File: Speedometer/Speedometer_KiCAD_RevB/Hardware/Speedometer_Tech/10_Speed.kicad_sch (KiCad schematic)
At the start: 14 parts, among them U100 TLC59108IPWR, U101 TLC59108IPWR, U102 TLC59108IPWR, U110 TLC59108IPWR, U111 TLC59108IPWR

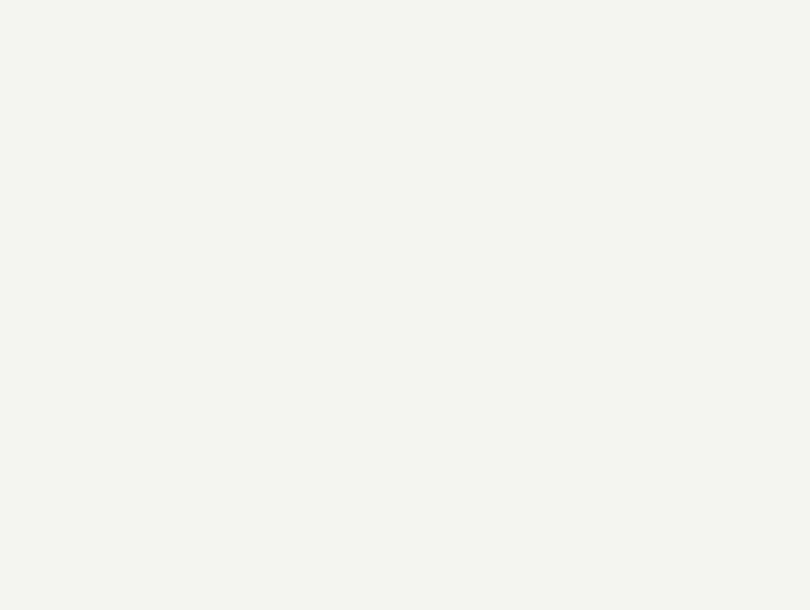
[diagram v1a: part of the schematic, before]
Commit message: current version of lada speedometer in kicad
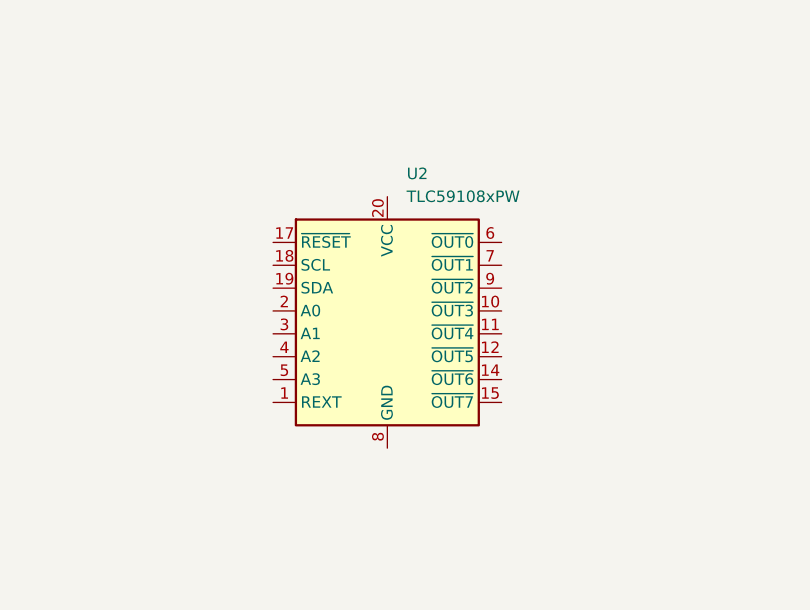
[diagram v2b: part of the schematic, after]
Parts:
- added U2: TLC59108xPW, Package_SO:TSSOP-20_4.4x6.5mm_P0.65mm, symbol Driver_LED:TLC59108xPW
- U100, U101, U102, U110, U111: footprint PW0020A_M -> Package_SO:TSSOP-20_4.4x6.5mm_P0.65mm
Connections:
- new net: U2.13 (GND), U2.16 (GND), U2.8 (GND)
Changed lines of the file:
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@@
 			)
 		)
-		(property "Footprint" "PW0020A_M"
+		(property "Footprint" "Package_SO:TSSOP-20_4.4x6.5mm_P0.65mm"
 			(at 68.58 109.0422 0)
 			(effects
@@
 			)
 		)
-		(property "Footprint" "PW0020A_M"
+		(property "Footprint" "Package_SO:TSSOP-20_4.4x6.5mm_P0.65mm"
 			(at 170.18 109.0422 0)
 			(effects
@@
 	)
 	(symbol
+		(lib_id "Driver_LED:TLC59108xPW")
+		(at 231.14 217.17 0)
+		(unit 1)
+		(exclude_from_sim no)
+		(in_bom yes)
+		(on_board yes)
+		(dnp no)
+		(fields_autoplaced yes)
+		(property "Reference" "U2"
+			(at 233.2833 199.39 0)
+			(effects
+				(font
+					(size 1.27 1.27)
+				)
+				(justify left)
+			)
+		)
+		(property "Value" "TLC59108xPW"
+			(at 233.2833 201.93 0)
+			(effects
+				(font
+					(size 1.27 1.27)
+				)
+				(justify left)
+			)
+		)
+		(property "Footprint" "Package_SO:TSSOP-20_4.4x6.5mm_P0.65mm"
+			(at 231.14 217.17 0)
+			(effects
+				(font
+					(size 1.27 1.27)
+				)
+				(hide yes)
+			)
+		)
+		(property "Datasheet" "https://www.ti.com/lit/ds/symlink/tlc59108.pdf"
+			(at 226.06 218.44 0)
+			(effects
+				(font
+					(size 1.27 1.27)
+				)
+				(hide yes)
+			)
+		)
+		(property "Description" "8-Channel, 8-Bit Fm+ I2C-Bus Constant-Current LED Sink Driver, TSSOP-20"
+			(at 231.14 217.17 0)
+			(effects
+				(font
+					(size 1.27 1.27)
+				)
+				(hide yes)
+			)
+		)
+		(pin "12"
+		)
+		(pin "8"
+		)
+		(pin "19"
+		)
+		(pin "2"
+		)
+		(pin "3"
+		)
+		(pin "4"
+		)
+		(pin "5"
+		)
+		(pin "1"
+		)
+		(pin "20"
+		)
+		(pin "13"
+		)
+		(pin "14"
+		)
+		(pin "10"
+		)
+		(pin "11"
+		)
+		(pin "9"
+		)
+		(pin "7"
+		)
+		(pin "6"
+		)
+		(pin "15"
+		)
+		(pin "17"
+		)
+		(pin "18"
+		)
+		(pin "16"
+		)
+		(instances
+			(project ""
+				(path "/7a911dfa-7957-409a-ad31-10c26a0bf949/7f25a167-5e25-4142-beba-23f2a558c57e"
+					(reference "U2")
+					(unit 1)
+				)
+			)
+		)
+	)
+	(symbol
 		(lib_id "Speedometer_Tech-altium-import:Designator_0_TI-TLC59108PW20")
 		(at 99.06 228.4222 0)
@@
 			)
 		)
-		(property "Footprint" "PW0020A_M"
+		(property "Footprint" "Package_SO:TSSOP-20_4.4x6.5mm_P0.65mm"
 			(at 99.06 228.4222 0)
 			(effects
@@
 			)
 		)
-		(property "Footprint" "PW0020A_M"
+		(property "Footprint" "Package_SO:TSSOP-20_4.4x6.5mm_P0.65mm"
 			(at 269.24 109.0422 0)
 			(effects
@@
 			)
 		)
-		(property "Footprint" "PW0020A_M"
+		(property "Footprint" "Package_SO:TSSOP-20_4.4x6.5mm_P0.65mm"
 			(at 99.06 190.3222 0)
 			(effects

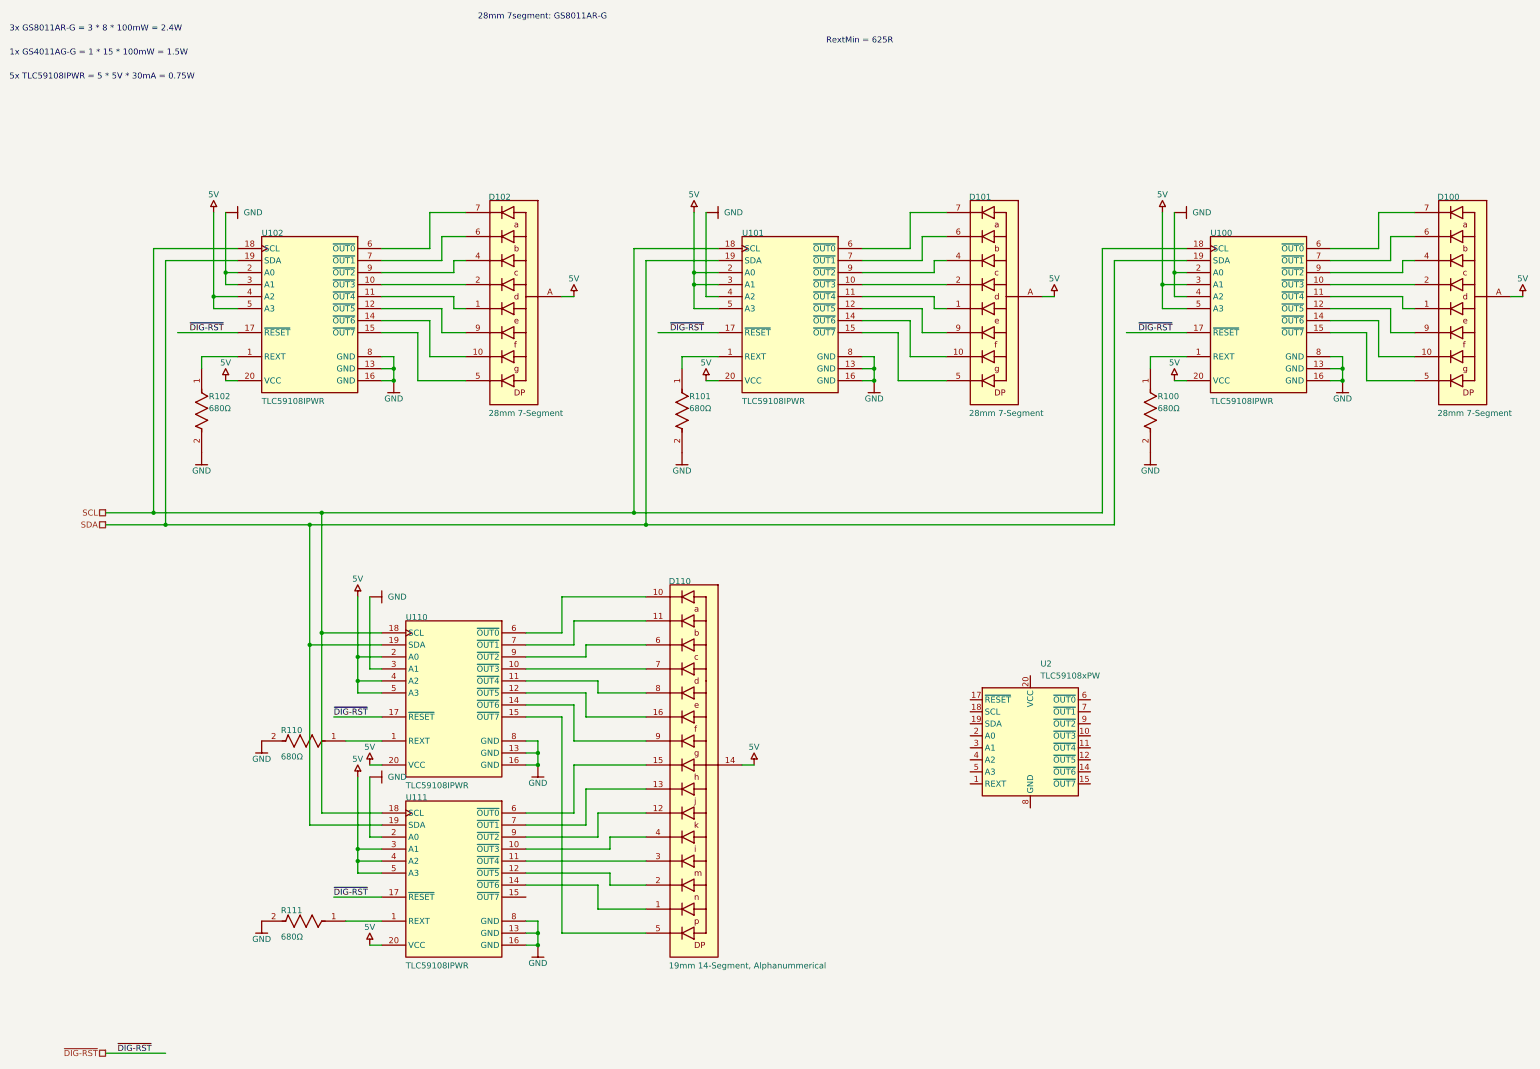
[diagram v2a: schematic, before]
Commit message: Speedometer DRC mostly passed
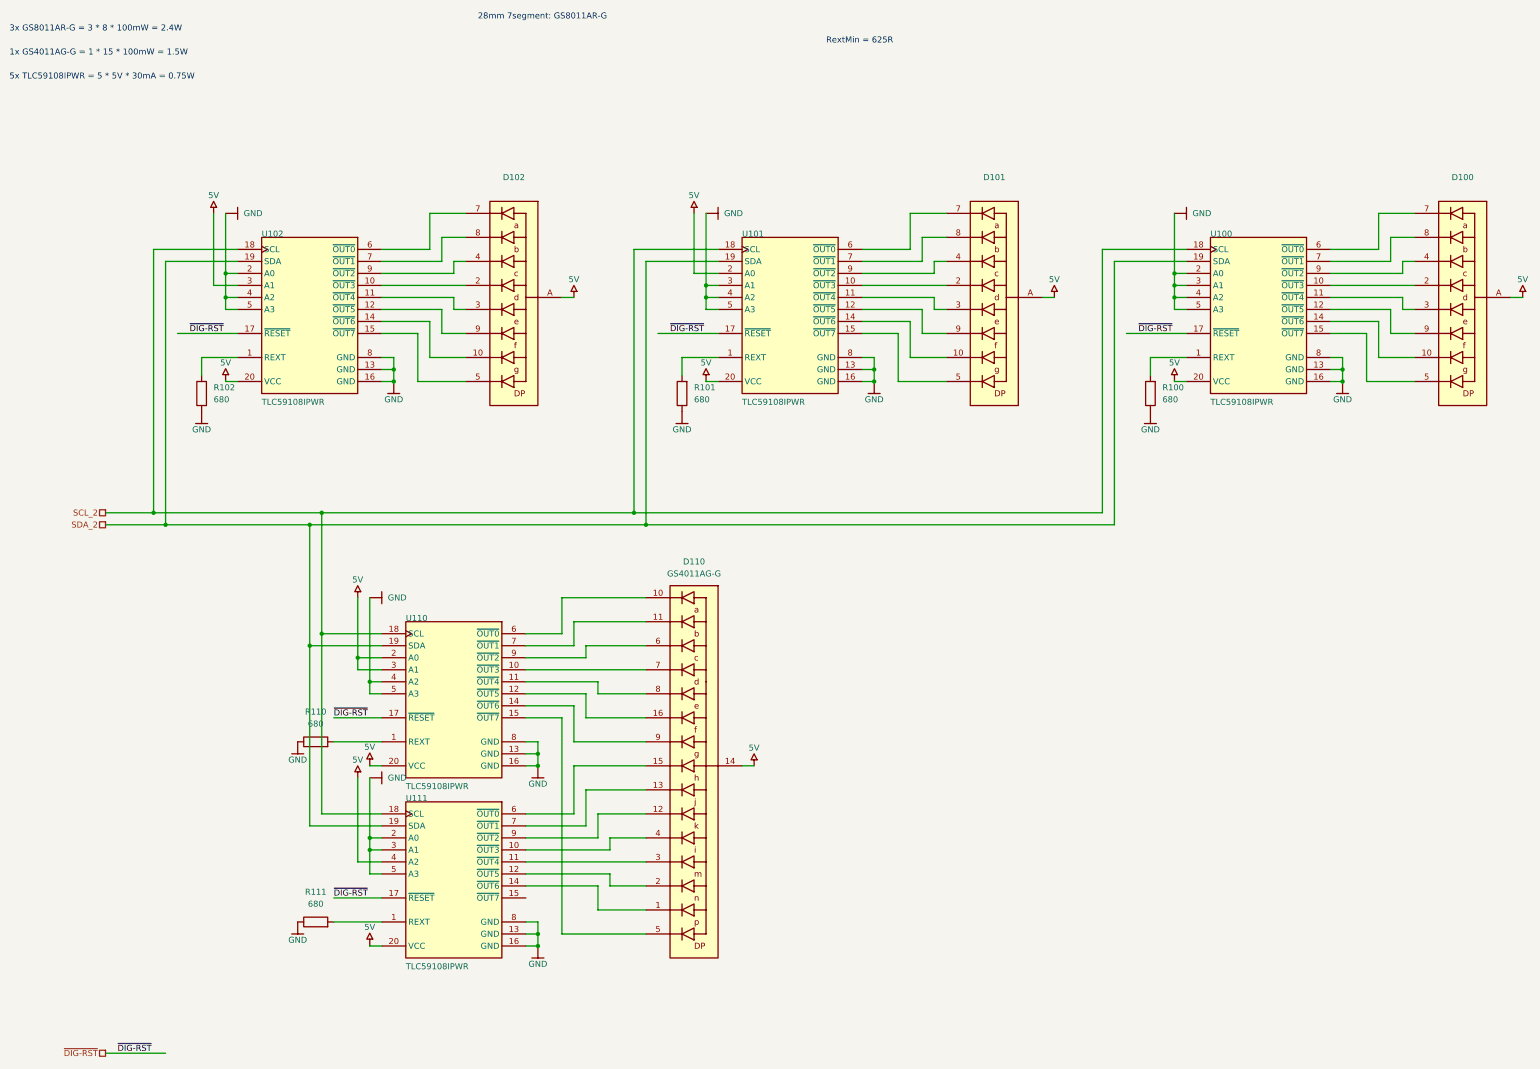
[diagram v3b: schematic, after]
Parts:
- removed D100, D101, D102: 28mm 7-Segment, GS8011AR-G, symbol Speedometer_Tech-altium-import:Designator_2_GS8011AR-G
- removed D110: 19mm 14-Segment, Alphanummerical, GS4011AG-G, symbol Speedometer_Tech-altium-import:Designator_2_GS4011AG-G
- removed R100, R101, R102: 680Ω, FP-CRCW0603-e3-IPC_A, symbol Speedometer_Tech-altium-import:Designator_3_1029c3af85768c4190bb7ad29bc67b5
- removed R110, R111: 680Ω, FP-CRCW0603-e3-IPC_A, symbol Speedometer_Tech-altium-import:Designator_2_1029c3af85768c4190bb7ad29bc67b5
- removed U2: TLC59108xPW, Package_SO:TSSOP-20_4.4x6.5mm_P0.65mm, symbol Driver_LED:TLC59108xPW
- added D100, D101, D102: ~, Display_7Segment:GS8011AR-G, symbol LED:GS8011AR-G
- added D110: GS4011AG-G, Display_7Segment:GS4011AG-G, symbol LED:GS4011AG-G
- added R100, R101, R102, R110, R111: 680, Resistor_SMD:R_0603_1608Metric, symbol Device:R
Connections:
- net 5V: now also U102.3 (A1), U110.3 (A1), D100.A, D101.A, D102.A, D110.14; no longer U100.3 (A1), U100.5 (A3), U101.3 (A1), U101.5 (A3), U102.4 (A2), U102.5 (A3), U110.4 (A2), U110.5 (A3), U111.3 (A1), U111.5 (A3)
- net GND: now also U100.3 (A1), U100.5 (A3), U101.3 (A1), U101.5 (A3), U102.4 (A2), U102.5 (A3), U110.4 (A2), U110.5 (A3), U111.3 (A1), U111.5 (A3), R100.1, R101.1, R102.1, R110.1, R111.1; no longer U102.3 (A1), U110.3 (A1)
- net at U100.1 (REXT): now also R100.2
- net at U101.11 (~{OUT4}): now also D101.3
- net at U101.14 (~{OUT6}): now also D101.10
- net at U101.10 (~{OUT3}): now also D101.2
- net at U101.9 (~{OUT2}): now also D101.4
- net at U101.15 (~{OUT7}): now also D101.5
- net at U101.7 (~{OUT1}): now also D101.8
- net at U101.6 (~{OUT0}): now also D101.7
- net at U101.12 (~{OUT5}): now also D101.9
- net at U102.1 (REXT): now also R102.2
- net at U102.10 (~{OUT3}): now also D102.2
- net at U102.11 (~{OUT4}): now also D102.3
- net at U102.12 (~{OUT5}): now also D102.9
- net at U102.14 (~{OUT6}): now also D102.10
- net at U102.15 (~{OUT7}): now also D102.5
- net at U102.6 (~{OUT0}): now also D102.7
- net at U102.7 (~{OUT1}): now also D102.8
- net at U102.9 (~{OUT2}): now also D102.4
- net at U101.1 (REXT): now also R101.2
- net at U110.1 (REXT): now also R110.2
- net at U100.11 (~{OUT4}): now also D100.3
- net at U100.14 (~{OUT6}): now also D100.10
- net at U100.10 (~{OUT3}): now also D100.2
- net at U100.9 (~{OUT2}): now also D100.4
- net at U100.15 (~{OUT7}): now also D100.5
- net at U100.7 (~{OUT1}): now also D100.8
- net at U100.6 (~{OUT0}): now also D100.7
- net at U100.12 (~{OUT5}): now also D100.9
- net at U111.1 (REXT): now also R111.2
- net at U111.10 (~{OUT3}): now also D110.4
- net at U111.11 (~{OUT4}): now also D110.3
- net at U111.12 (~{OUT5}): now also D110.2
- net at U111.14 (~{OUT6}): now also D110.1
- net at U111.6 (~{OUT0}): now also D110.15
- net at U111.7 (~{OUT1}): now also D110.13
- net at U111.9 (~{OUT2}): now also D110.12
- net at U110.6 (~{OUT0}): now also D110.10
- net at U110.7 (~{OUT1}): now also D110.11
- net at U110.12 (~{OUT5}): now also D110.16
- net at U110.15 (~{OUT7}): now also D110.5
- net at U110.9 (~{OUT2}): now also D110.6
- net at U110.10 (~{OUT3}): now also D110.7
- net at U110.11 (~{OUT4}): now also D110.8
- net at U110.14 (~{OUT6}): now also D110.9
- net SCL renamed SCL_2
- net SDA renamed SDA_2
